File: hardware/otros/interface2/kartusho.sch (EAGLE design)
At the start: 13 parts, among them IC1 74HC174N, IC2 74HC32N, IC3 74HC133N, IC4 AM29F040S

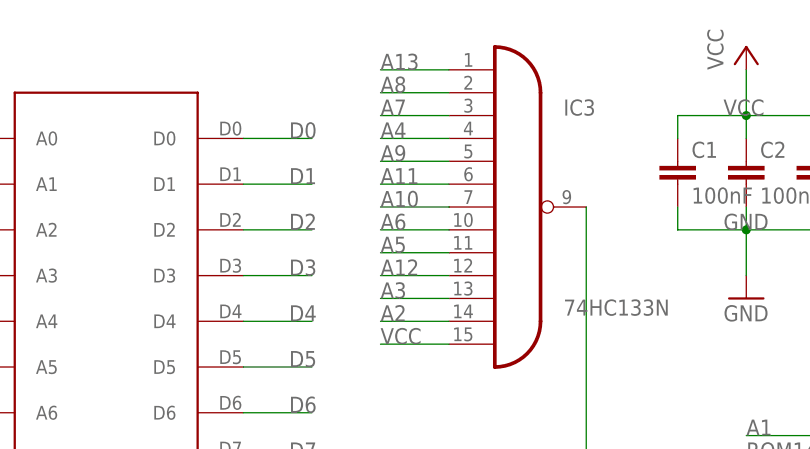
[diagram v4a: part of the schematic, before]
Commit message: 
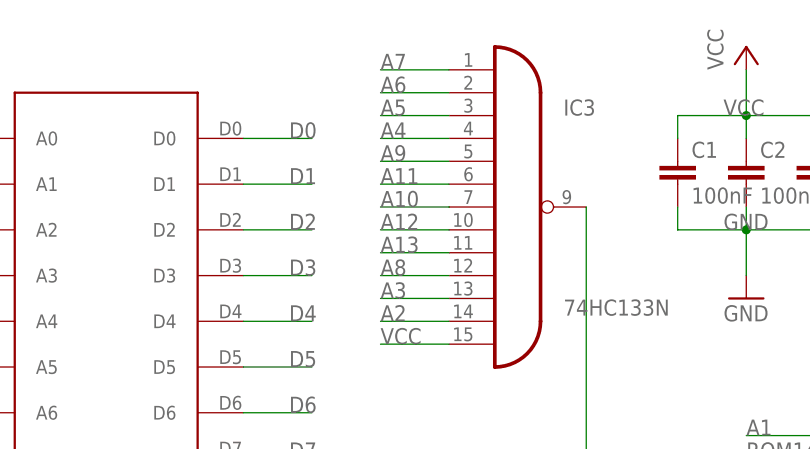
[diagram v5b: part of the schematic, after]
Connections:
- net A12: now also IC3A.I7; no longer IC3A.I9
- net A13: now also IC3A.I8; no longer IC3A.I0
- net A5: now also IC3A.I2; no longer IC3A.I8
- net A6: now also IC3A.I1; no longer IC3A.I7
- net A7: now also IC3A.I0; no longer IC3A.I2
- net A8: now also IC3A.I9; no longer IC3A.I1
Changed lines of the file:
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@@
 </segment>
 <segment>
-<wire x1="-10.16" y1="76.2" x2="-2.54" y2="76.2" width="0.1524" layer="91"/>
-<pinref part="IC3" gate="A" pin="I8"/>
-<label x="-10.16" y="76.2" size="1.778" layer="95"/>
+<wire x1="-10.16" y1="91.44" x2="-2.54" y2="91.44" width="0.1524" layer="91"/>
+<pinref part="IC3" gate="A" pin="I2"/>
+<label x="-10.16" y="91.44" size="1.778" layer="95"/>
 </segment>
 </net>
@@
 </segment>
 <segment>
-<wire x1="-10.16" y1="78.74" x2="-2.54" y2="78.74" width="0.1524" layer="91"/>
-<pinref part="IC3" gate="A" pin="I7"/>
-<label x="-10.16" y="78.74" size="1.778" layer="95"/>
+<wire x1="-10.16" y1="93.98" x2="-2.54" y2="93.98" width="0.1524" layer="91"/>
+<pinref part="IC3" gate="A" pin="I1"/>
+<label x="-10.16" y="93.98" size="1.778" layer="95"/>
 </segment>
 </net>
@@
 </segment>
 <segment>
-<wire x1="-10.16" y1="91.44" x2="-2.54" y2="91.44" width="0.1524" layer="91"/>
-<pinref part="IC3" gate="A" pin="I2"/>
-<label x="-10.16" y="91.44" size="1.778" layer="95"/>
+<pinref part="IC3" gate="A" pin="I0"/>
+<wire x1="-10.16" y1="96.52" x2="-2.54" y2="96.52" width="0.1524" layer="91"/>
+<label x="-10.16" y="96.52" size="1.778" layer="95"/>
 </segment>
 </net>
@@
 </segment>
 <segment>
-<wire x1="-10.16" y1="93.98" x2="-2.54" y2="93.98" width="0.1524" layer="91"/>
-<pinref part="IC3" gate="A" pin="I1"/>
-<label x="-10.16" y="93.98" size="1.778" layer="95"/>
+<wire x1="-10.16" y1="73.66" x2="-2.54" y2="73.66" width="0.1524" layer="91"/>
+<pinref part="IC3" gate="A" pin="I9"/>
+<label x="-10.16" y="73.66" size="1.778" layer="95"/>
 </segment>
 </net>
@@
 </segment>
 <segment>
-<wire x1="-10.16" y1="73.66" x2="-2.54" y2="73.66" width="0.1524" layer="91"/>
-<pinref part="IC3" gate="A" pin="I9"/>
-<label x="-10.16" y="73.66" size="1.778" layer="95"/>
+<wire x1="-10.16" y1="78.74" x2="-2.54" y2="78.74" width="0.1524" layer="91"/>
+<pinref part="IC3" gate="A" pin="I7"/>
+<label x="-10.16" y="78.74" size="1.778" layer="95"/>
 </segment>
 </net>
@@
 </segment>
 <segment>
-<pinref part="IC3" gate="A" pin="I0"/>
-<wire x1="-10.16" y1="96.52" x2="-2.54" y2="96.52" width="0.1524" layer="91"/>
-<label x="-10.16" y="96.52" size="1.778" layer="95"/>
+<wire x1="-10.16" y1="76.2" x2="-2.54" y2="76.2" width="0.1524" layer="91"/>
+<pinref part="IC3" gate="A" pin="I8"/>
+<label x="-10.16" y="76.2" size="1.778" layer="95"/>
 </segment>
 </net>

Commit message: 
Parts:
- C1: device rcl:C-EU025-025X050 -> rcl:C-EU050-025X075
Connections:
- net A10: now also IC3A.I4; no longer IC3A.I6
- net A11: now also IC3A.I7; no longer IC3A.I5
- net A12: now also IC3A.I9; no longer IC3A.I7
- net A13: now also IC3A.I11; no longer IC3A.I8
- net A2: now also IC3A.I6; no longer IC3A.I11
- net A3: now also IC3A.I5; no longer IC3A.I10
- net A8: now also IC3A.I10; no longer IC3A.I9
- net A9: now also IC3A.I8; no longer IC3A.I4
- net CS: now also IC2C.I1; no longer IC2C.I0
- net LOCK: now also IC2C.I0; no longer IC2C.I1
- net N$3: now also IC2A.I1; no longer IC2A.I0
- net N$4: now also IC2A.I0; no longer IC2A.I1
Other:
- moved on the sheet: IC2A

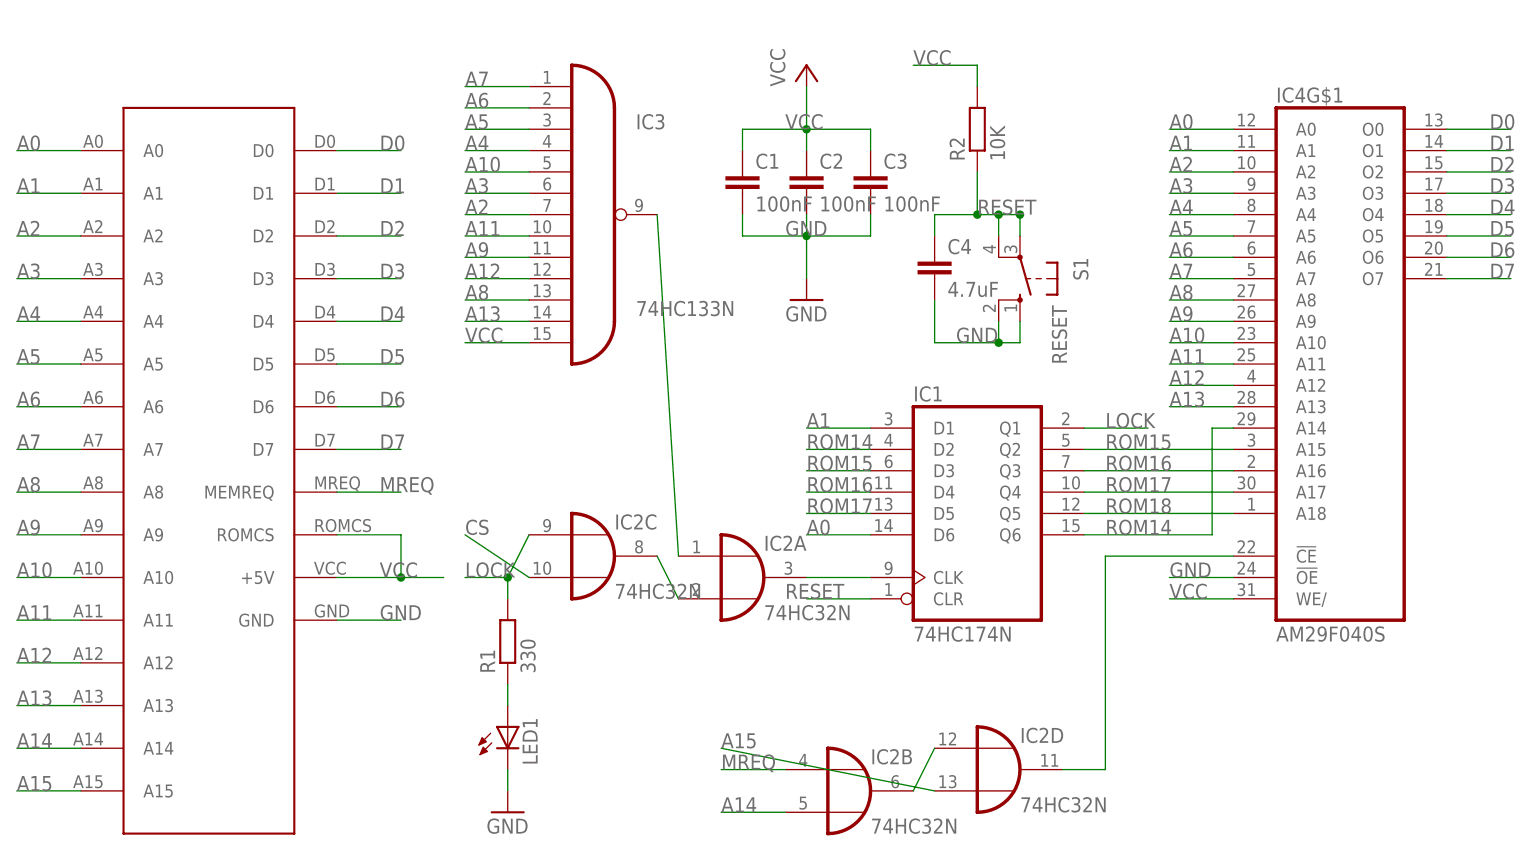
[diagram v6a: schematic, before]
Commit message: 
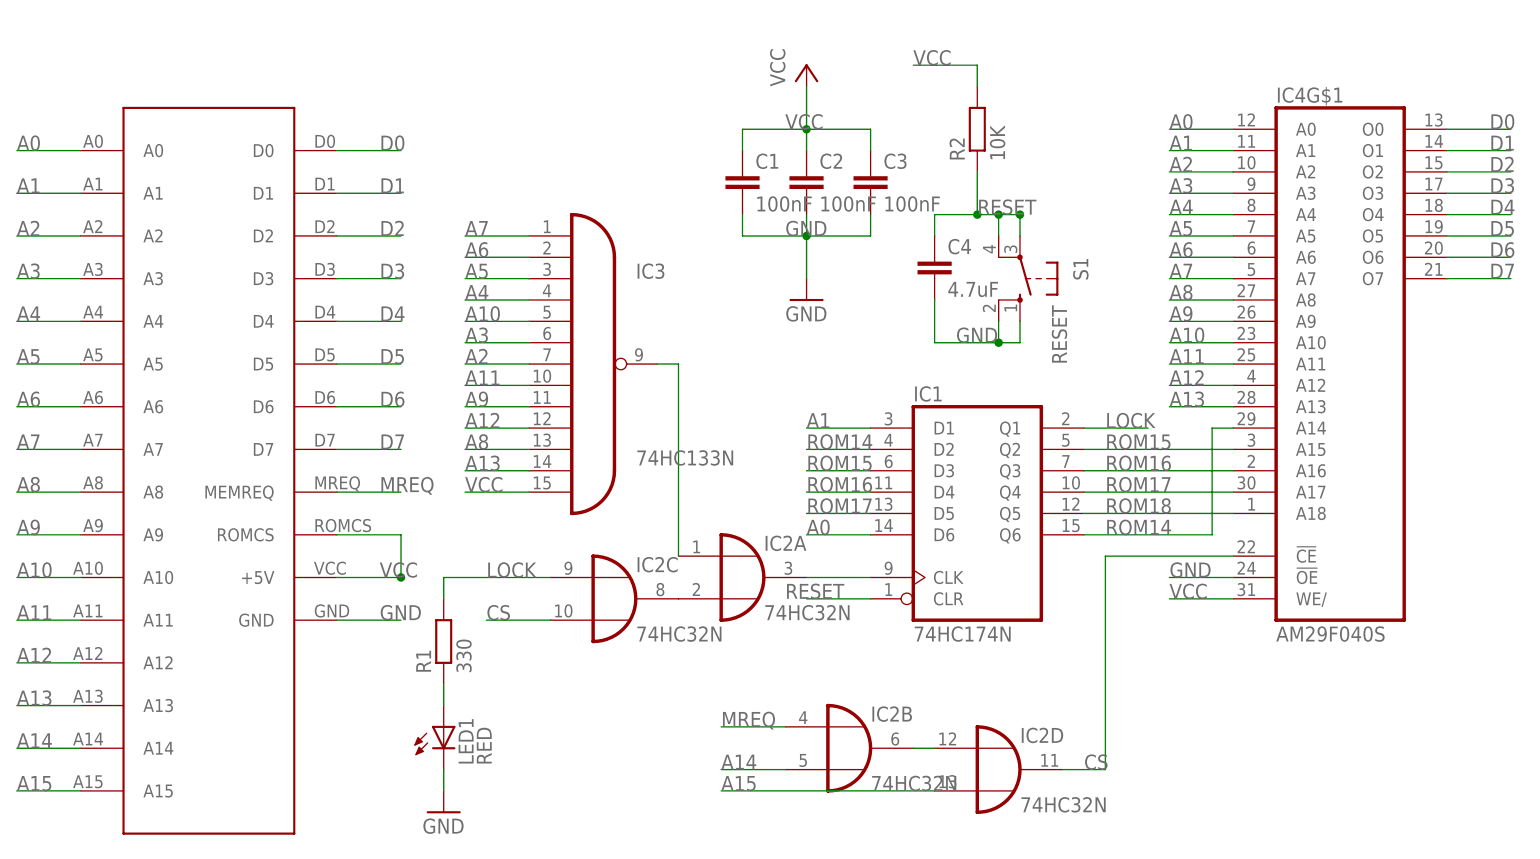
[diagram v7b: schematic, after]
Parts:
- LED1: value (none) -> RED
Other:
- moved on the sheet: IC2B, IC2C, IC3, LED1, R1
